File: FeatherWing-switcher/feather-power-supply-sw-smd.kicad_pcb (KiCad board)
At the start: 2 copper layers, 22.9 x 50.8 mm, 24 parts, among them J1 5.08mm, J2 Conn_01x12, J3 Conn_01x16, U1 TPS5405DR

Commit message: update mounting holes
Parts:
- H1, H2: value MountingHole -> MountingHole_Pad; footprint MountingHole:MountingHole_2.7mm_M2.5 -> MountingHole:MountingHole_2.5mm_Pad
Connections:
- net A0 renamed A1
- H1 pad 1: (no net) -> GND
- H2 pad 1: (no net) -> GND
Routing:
- net GND: vias 29 -> 27

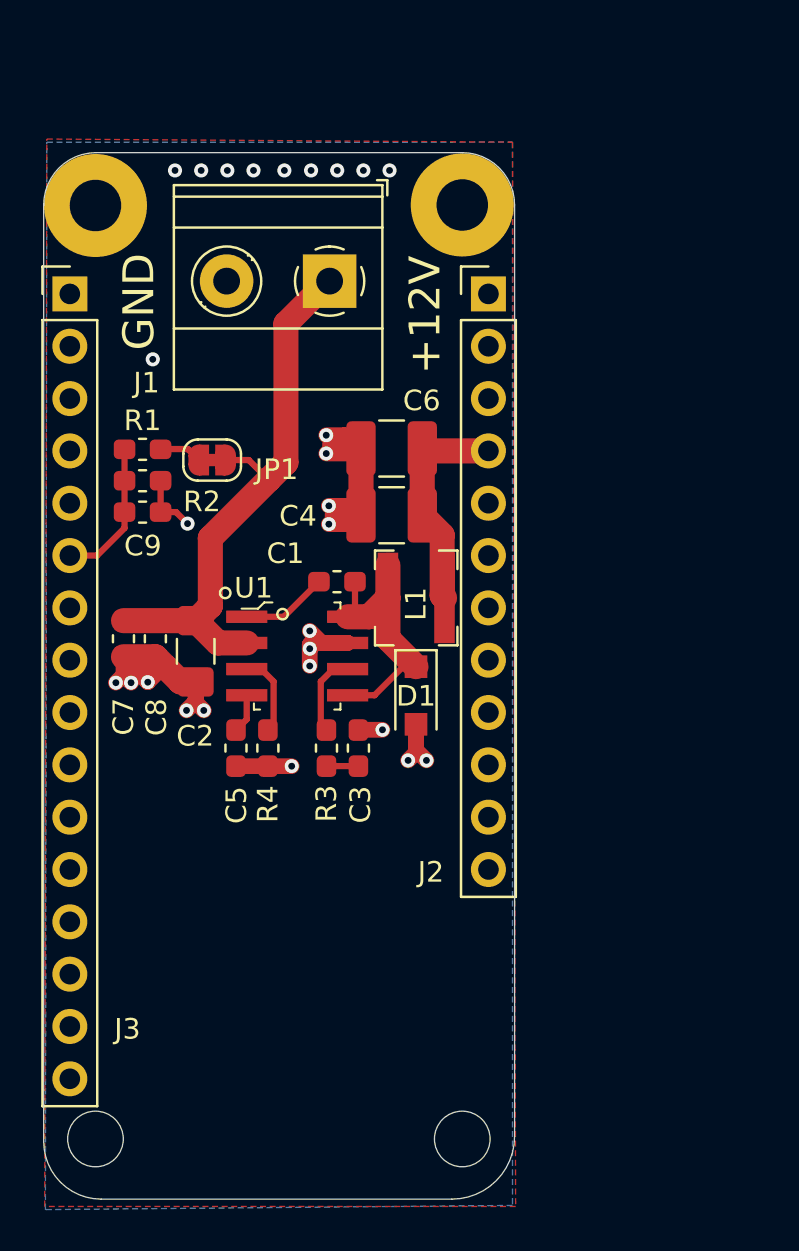
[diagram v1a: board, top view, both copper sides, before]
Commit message: adds qwicc conn
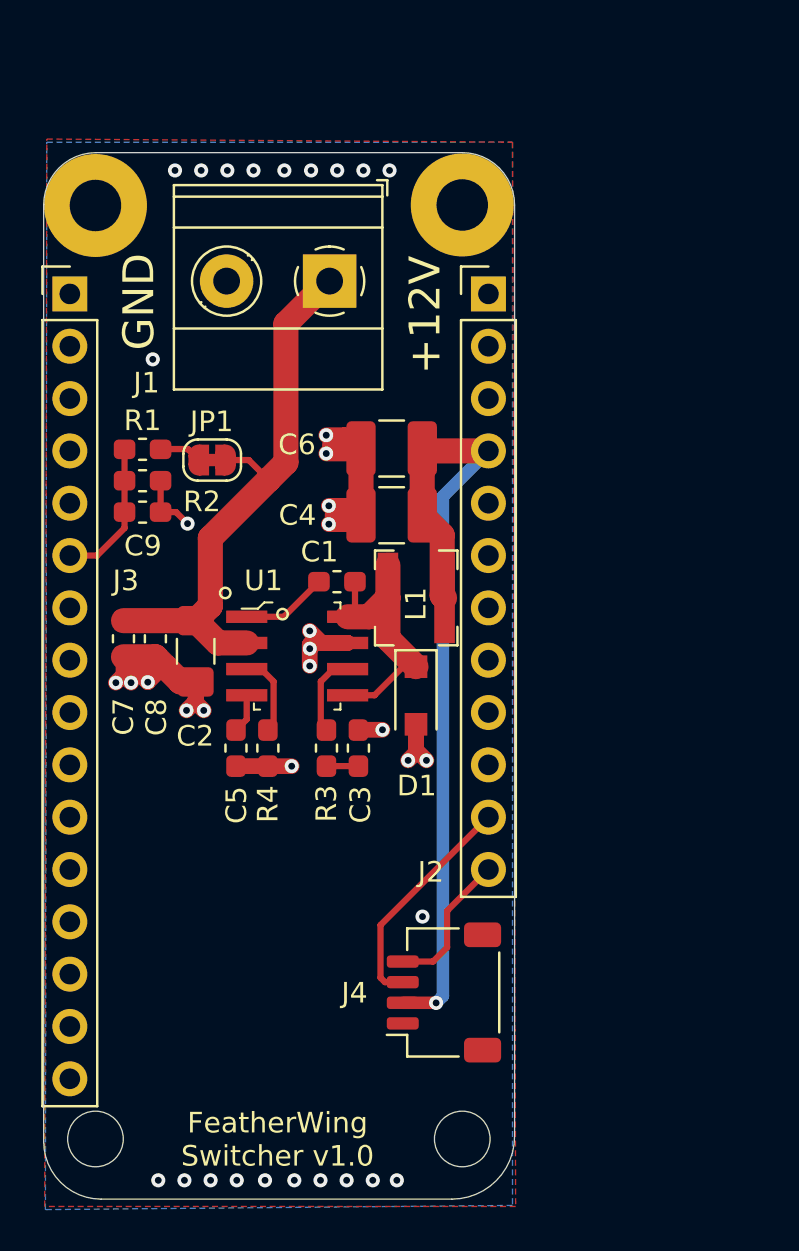
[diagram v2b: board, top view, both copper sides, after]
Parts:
- added J4: QWIIC, Connector_JST:JST_SH_SM04B-SRSS-TB_1x04-1MP_P1.00mm_Horizontal, F.Cu at (136.0, 104.6)
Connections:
- net A1 renamed /A1
- net Net-(J2-Pad2) renamed +3V3
- J2 pad 11: Net-(J2-Pad11) -> /SCL
- J2 pad 12: Net-(J2-Pad12) -> /SDA
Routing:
- net VUSB: track 11.0 -> 40.4 mm, vias 0 -> 1
- net /SCL: track 0.00 -> 11.1 mm
- net /SDA: track 0.00 -> 7.05 mm
- net GND: vias 27 -> 38
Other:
- board text added: "FeatherWing Switcher v1.0"
- board text added: "JFSaraceno 09/2020"

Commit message: adds proto and leds
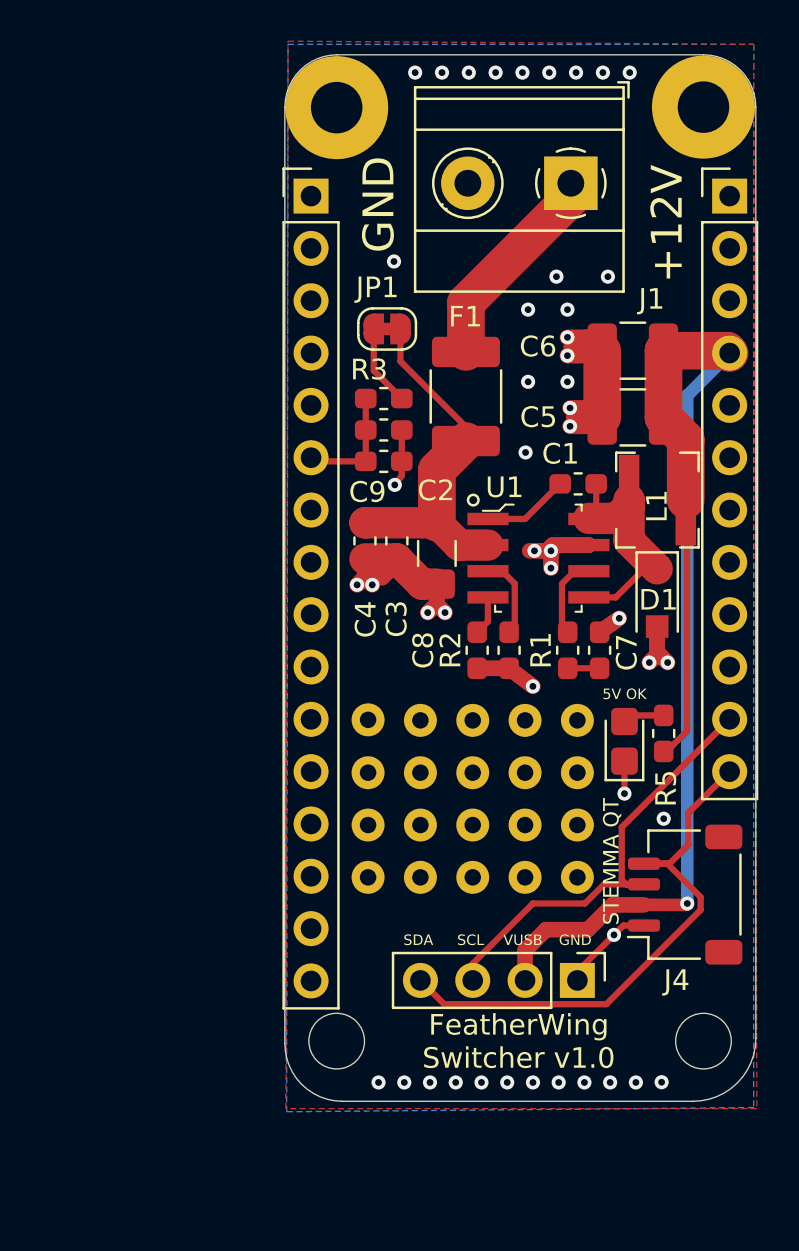
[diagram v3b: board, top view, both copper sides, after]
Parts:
- added D2: 5V OK, LED_SMD:LED_0805_2012Metric_Castellated, F.Cu at (144.8, 92.5)
- added F1: 24V 1.1A, Fuse:Fuse_1812_4532Metric_Castellated, F.Cu at (137.1, 75.7)
- added J5: Conn_01x04, Connector_PinHeader_2.54mm:PinHeader_1x04_P2.54mm_Vertical, F.Cu at (142.5, 104.1)
- added LOGO1: Logo_Open_Hardware_Small, Symbol:OSHW-Symbol_6.7x6mm_SilkScreen, B.Cu at (135.7, 72.9)
- added R5: 330, Resistor_SMD:R_0603_1608Metric_Pad1.05x0.95mm_HandSolder, F.Cu at (146.7, 92.1)
- added REF**: Prototype_05x05_P2.54mm_Vertical, FeatherWing-switcher:Prototype_P2.54mm_Vertical, F.Cu at (137.4, 95.2)
- added REF**: KiCad-Logo2_5mm_SilkScreen, Symbol:KiCad-Logo2_5mm_SilkScreen, B.Cu at (138.4, 85.1)
- C3: value 10nF -> 1uF
- C4: value 22uF -> 0.1uF; footprint Capacitor_SMD:C_1210_3225Metric_Pad1.42x2.65mm_HandSolder -> Capacitor_SMD:C_0603_1608Metric_Pad1.05x0.95mm_HandSolder
- C5: value 10nF -> 22uF; footprint Capacitor_SMD:C_0603_1608Metric_Pad1.05x0.95mm_HandSolder -> Capacitor_SMD:C_1210_3225Metric_Pad1.42x2.65mm_HandSolder
- C7: value 1uF -> 10nF
- C8: value 0.1uF -> 10nF
- R1: value 27k/0.1% -> 10k
- R2: value 3k/0.1% -> 100K*
- R3: value 10k -> 1M/0.1%
- R4: value 100k* -> 100K/0.1%
- moved C5 25.1 mm to (145.2, 76.7), turned to 180 degrees
- moved C7 23.1 mm to (143.6, 88.0), turned to 90 degrees
- moved R1 22.8 mm to (142.0, 88.0), turned to 270 degrees
- moved R2 19.6 mm to (139.2, 88.0), turned to 270 degrees
- moved R3 17.2 mm to (133.1, 75.8), turned to 0 degrees
- moved R4 16.4 mm to (133.1, 77.3), turned to 0 degrees
- moved C8 15.6 mm to (137.6, 88.0)
- moved C1 12.6 mm to (142.5, 80.0)
- moved D1 12.6 mm to (146.4, 85.5)
- moved J2 12.6 mm to (149.9, 66.0)
- moved J3 12.6 mm to (129.6, 66.0)
- moved C2 12.6 mm to (135.7, 83.3)
- moved J1 12.6 mm to (142.2, 65.4)
- moved J4 12.6 mm to (147.7, 99.9)
- moved H4 12.6 mm to (130.8, 107.0)
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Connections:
- C2 pad 1: /BATT+ -> /VIN
- C3 pad 1: Net-(C3-Pad1) -> /VIN
- C4 pad 1: VUSB -> /VIN
- C5 pad 1: Net-(C5-Pad1) -> VUSB
- C7 pad 1: /BATT+ -> Net-(C7-Pad1)
- C8 pad 1: /BATT+ -> Net-(C8-Pad1)
- J1 pad 1: /BATT+ -> Net-(F1-Pad1)
- JP1 pad 1: /BATT+ -> /VIN
- R1 pad 1: /A1 -> Net-(R1-Pad1)
- R1 pad 2: Net-(JP1-Pad2) -> Net-(C7-Pad1)
- R2 pad 1: /A1 -> /ROSC
- R3 pad 1: Net-(R3-Pad1) -> /A1
- R3 pad 2: Net-(C3-Pad1) -> Net-(JP1-Pad2)
- R4 pad 1: /ROSC -> /A1
- U1 pad 2: /BATT+ -> /VIN
- U1 pad 4: Net-(C5-Pad1) -> Net-(C8-Pad1)
- U1 pad 6: Net-(R3-Pad1) -> Net-(R1-Pad1)
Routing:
- net /BATT+: track 28.1 -> 0.00 mm
- net VUSB: track 40.4 -> 61.6 mm
- net /SDA: track 7.05 -> 26.9 mm
- net /VIN: track 0.00 -> 17.7 mm
- net /SCL: track 11.1 -> 21.9 mm
- net Net-(F1-Pad1): track 0.00 -> 10.3 mm
- net Net-(R1-Pad1): track 0.00 -> 4.03 mm
- net Net-(R3-Pad1): track 4.03 -> 0.00 mm
- net GND: track 44.4 -> 47.8 mm, vias 38 -> 48
- net Net-(D2-Pad2): track 0.00 -> 1.94 mm
- net Net-(C8-Pad1): track 0.00 -> 1.91 mm
- net Net-(C5-Pad1): track 1.91 -> 0.00 mm
- net Net-(JP1-Pad2): track 2.08 -> 3.94 mm
- net Net-(C3-Pad1): track 1.57 -> 0.00 mm
- net Net-(C7-Pad1): track 0.00 -> 1.57 mm
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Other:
- rule via_min_drill: 0.3 -> 0.3302
- rule via_min_size: 0.4 -> 0.6858
- board text added: "SCL"
- board text added: "SDA"
- board text added: "STEMMA QT"
- board text added: "VUSB"

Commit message: major updates to route buses using  copper pours
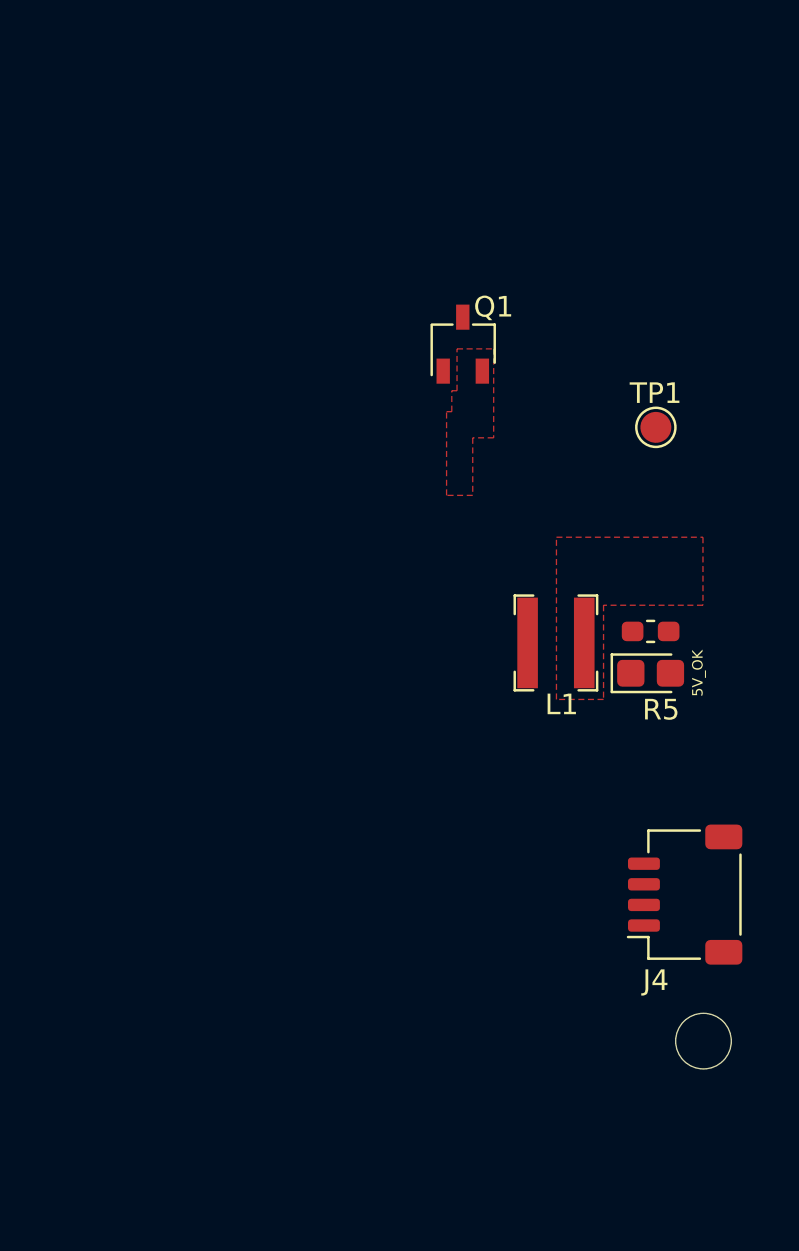
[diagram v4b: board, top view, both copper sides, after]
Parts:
- removed C1, C4: 0.1uF, Capacitor_SMD:C_0603_1608Metric_Pad1.05x0.95mm_HandSolder
- removed C2: 10uF, Capacitor_SMD:C_1206_3216Metric_Pad1.42x1.75mm_HandSolder
- removed C3: 1uF, Capacitor_SMD:C_0603_1608Metric_Pad1.05x0.95mm_HandSolder
- removed C5, C6: 22uF, Capacitor_SMD:C_1210_3225Metric_Pad1.42x2.65mm_HandSolder
- removed C7, C8, C9: 10nF, Capacitor_SMD:C_0603_1608Metric_Pad1.05x0.95mm_HandSolder
- removed D1: ~, Diode_SMD:D_SOD-123F
- removed F1: 24V 1.1A, Fuse:Fuse_1812_4532Metric_Castellated
- removed H1, H2: MountingHole_Pad, MountingHole:MountingHole_2.5mm_Pad
- removed H4: MountingHole, MountingHole:MountingHole_2.7mm_M2.5
- removed J1: 5.08mm, TerminalBlock_Phoenix:TerminalBlock_Phoenix_MKDS-1,5-2_1x02_P5.00mm_Horizontal
- removed J2: Conn_01x12, Connector_PinHeader_2.54mm:PinHeader_1x12_P2.54mm_Vertical
- removed J3: Conn_01x16, Connector_PinHeader_2.54mm:PinHeader_1x16_P2.54mm_Vertical
- removed JP1: SolderJumper_2_Bridged, Jumper:SolderJumper-2_P1.3mm_Bridged_RoundedPad1.0x1.5mm
- removed LOGO1: Logo_Open_Hardware_Small, Symbol:OSHW-Symbol_6.7x6mm_SilkScreen
- removed R1: 10k, Resistor_SMD:R_0603_1608Metric_Pad1.05x0.95mm_HandSolder
- removed R2: 100K*, Resistor_SMD:R_0603_1608Metric_Pad1.05x0.95mm_HandSolder
- removed R3: 1M/0.1%, Resistor_SMD:R_0603_1608Metric_Pad1.05x0.95mm_HandSolder
- removed R4: 100K/0.1%, Resistor_SMD:R_0603_1608Metric_Pad1.05x0.95mm_HandSolder
- removed the REF** at (137.4, 95.2)
- removed U1: TPS5405DR, digikey-footprints:SOIC-8_W3.9mm
- added Q1: Q_PMOS_GSD, Package_TO_SOT_SMD:TSOT-23, F.Cu at (136.9, 73.2)
- added TP1: TestPoint, TestPoint:TestPoint_Pad_D1.5mm, F.Cu at (146.3, 77.2)
- D2: value 5V OK -> 5V_OK
- J5: value Conn_01x04 -> 0.1
- R5: value 330 -> 1k
- moved L1 8.51 mm to (141.5, 87.7)
- moved R5 4.99 mm to (146.1, 87.1), turned to 0 degrees
- moved D2 3.54 mm to (146.1, 89.2), turned to 0 degrees
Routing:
- net VUSB: track 61.6 -> 0.00 mm, vias 1 -> 0
- net GND: track 47.8 -> 0.00 mm, vias 48 -> 0
- net /SDA: track 26.9 -> 0.00 mm
- net /SCL: track 21.9 -> 0.00 mm
- net /VIN: track 17.7 -> 0.00 mm
- net Net-(C1-Pad2): track 12.1 -> 0.00 mm
- net Net-(F1-Pad1): track 10.3 -> 0.00 mm
- net /A1: track 5.78 -> 0.00 mm
- net Net-(C1-Pad1): track 4.21 -> 0.00 mm
- net Net-(R1-Pad1): track 4.03 -> 0.00 mm
- net /ROSC: track 4.03 -> 0.00 mm
- net Net-(JP1-Pad2): track 3.94 -> 0.00 mm
- net Net-(D2-Pad2): track 1.94 -> 0.00 mm
- net Net-(C8-Pad1): track 1.91 -> 0.00 mm
- net Net-(C7-Pad1): track 1.57 -> 0.00 mm
- added copper zone on F.Cu, net VIN_SW
- added copper zone on F.Cu, net VUSB
- removed copper zone on B.Cu, net GND
- removed copper zone on F.Cu, net GND
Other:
- board outline removed
- board text removed: "+12V"
- board text removed: "FeatherWing Switcher v1.0"
- board text removed: "GND"
- board text removed: "JFSaraceno 09/2020"
- board text removed: "SCL"
- board text removed: "SDA"
- board text removed: "STEMMA QT"
- board text removed: "VUSB"
